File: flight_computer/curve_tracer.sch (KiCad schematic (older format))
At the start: 31 parts

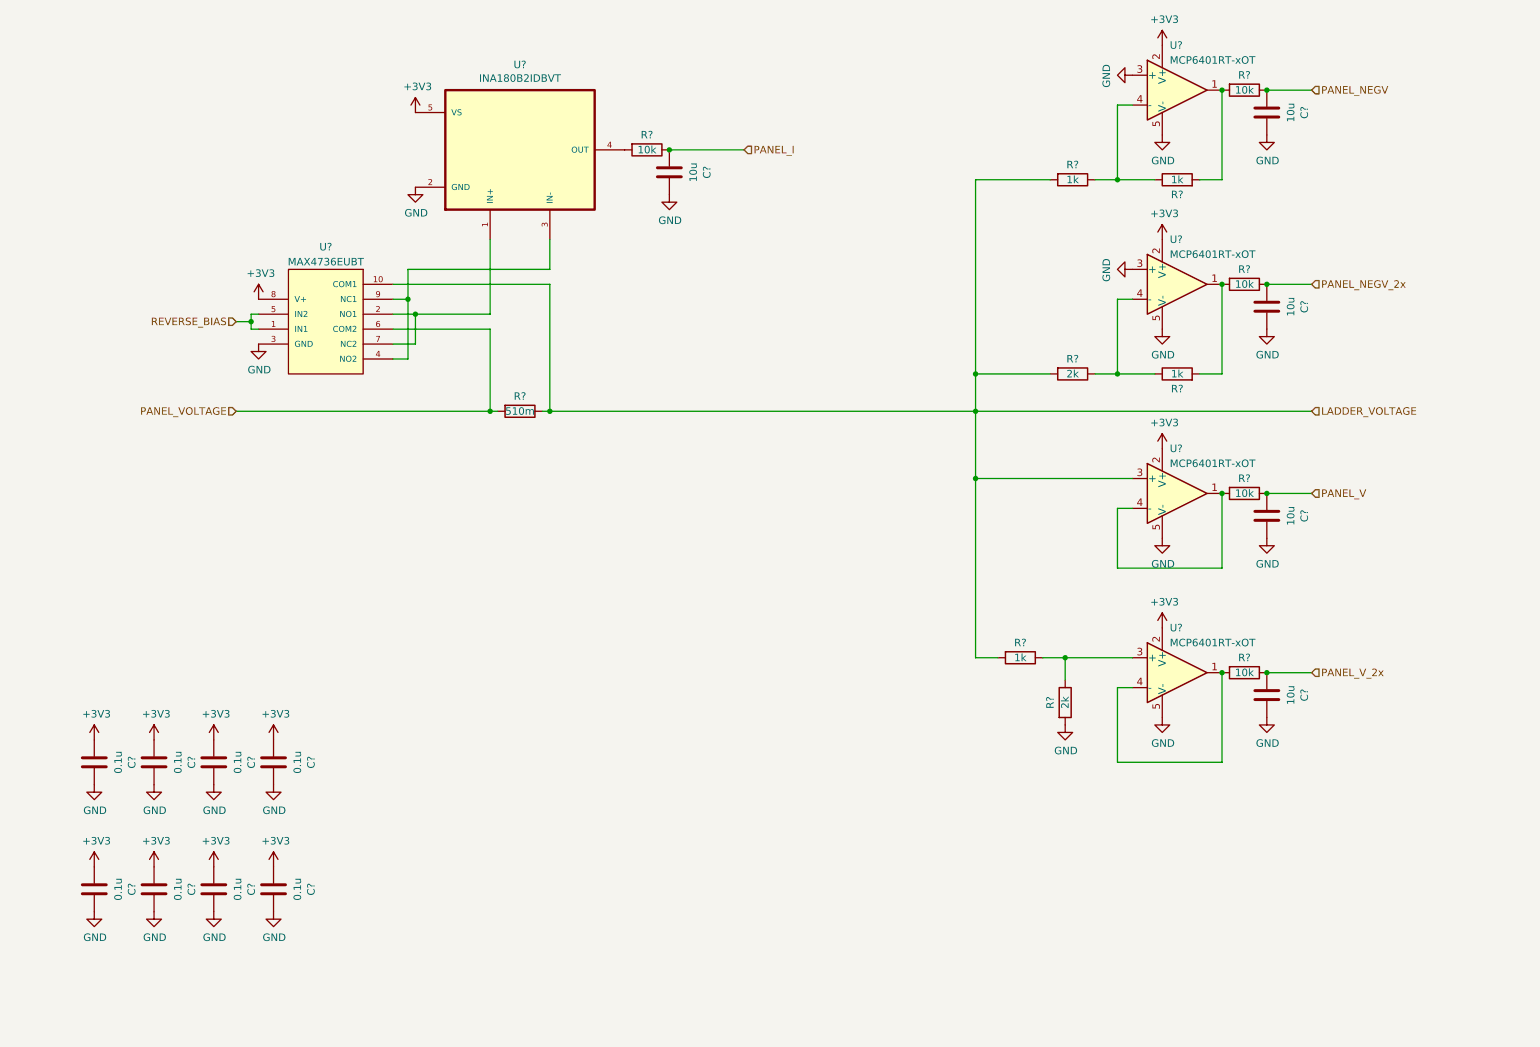
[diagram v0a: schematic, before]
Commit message: Updating flight computer
- Added datasheets for peripherals
- Added resistor ladder firmware
- Added perovskite switcher firmware
- Started flight computer firmware
- Added curve comparisons
- Updating flight computer schematic
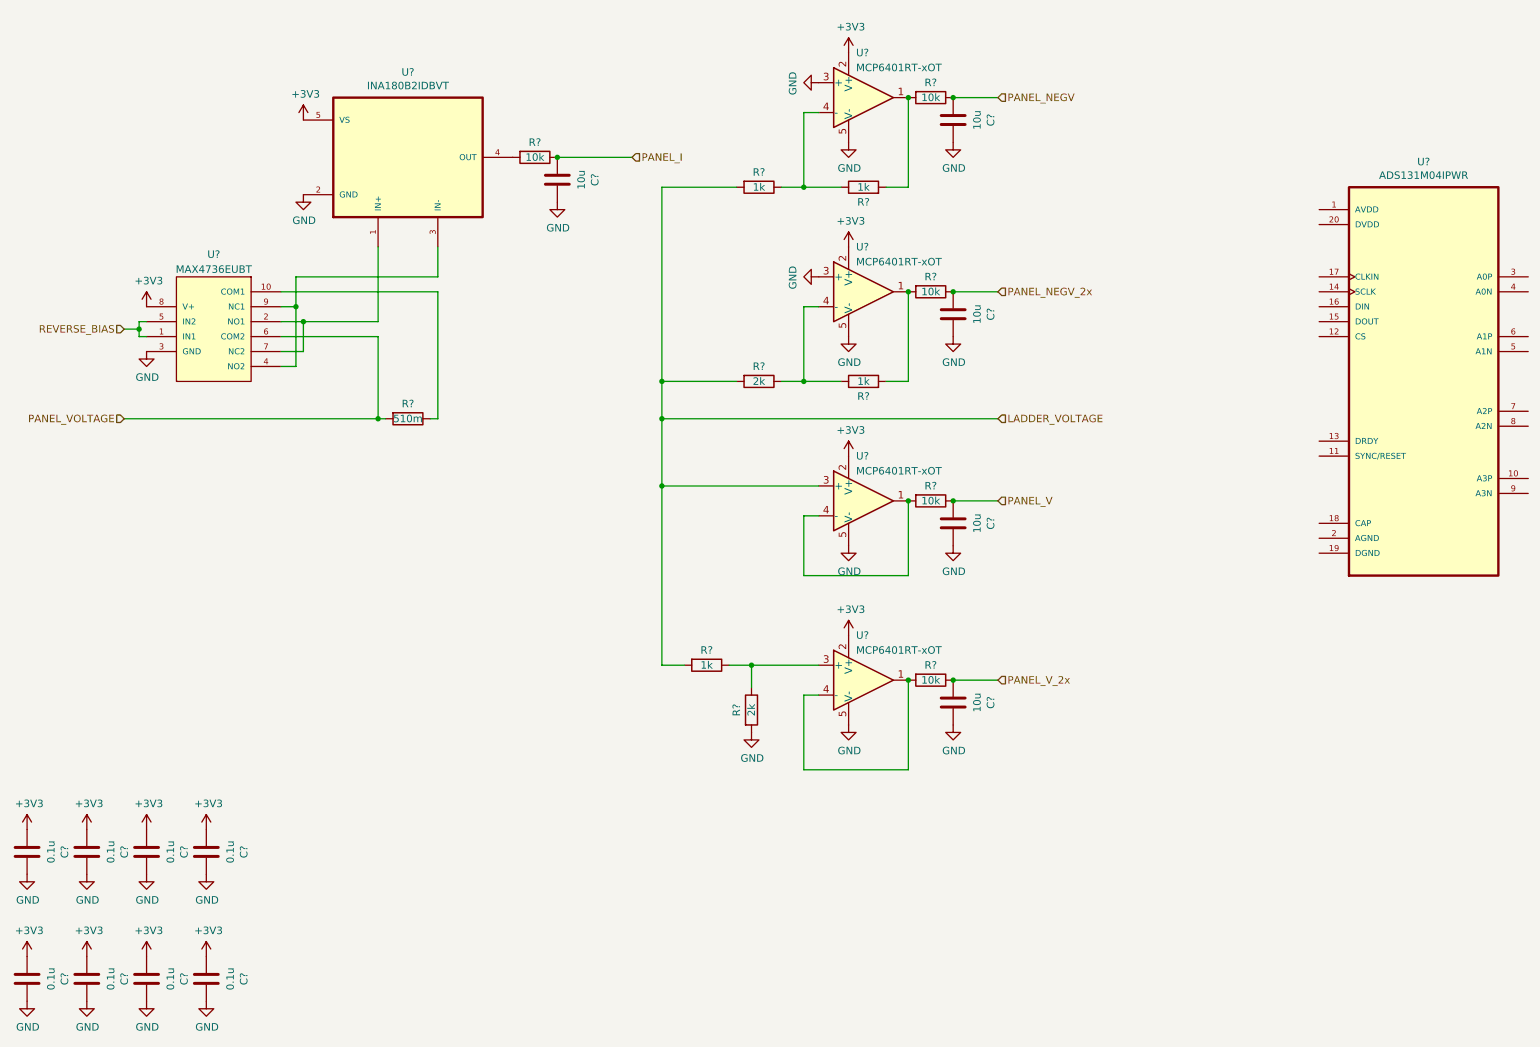
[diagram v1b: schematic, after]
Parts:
- added U?: ADS131M04IPWR, SOP65P640X120-20N, symbol ADS131M04IPWR:ADS131M04IPWR
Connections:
- net LADDER_VOLTAGE: no longer R?.1, U?.10 (COM1)
- new net: R?.1, U?.10 (COM1)
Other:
- moved on the sheet: C?, R?, U?

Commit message: Update flight computer schematic
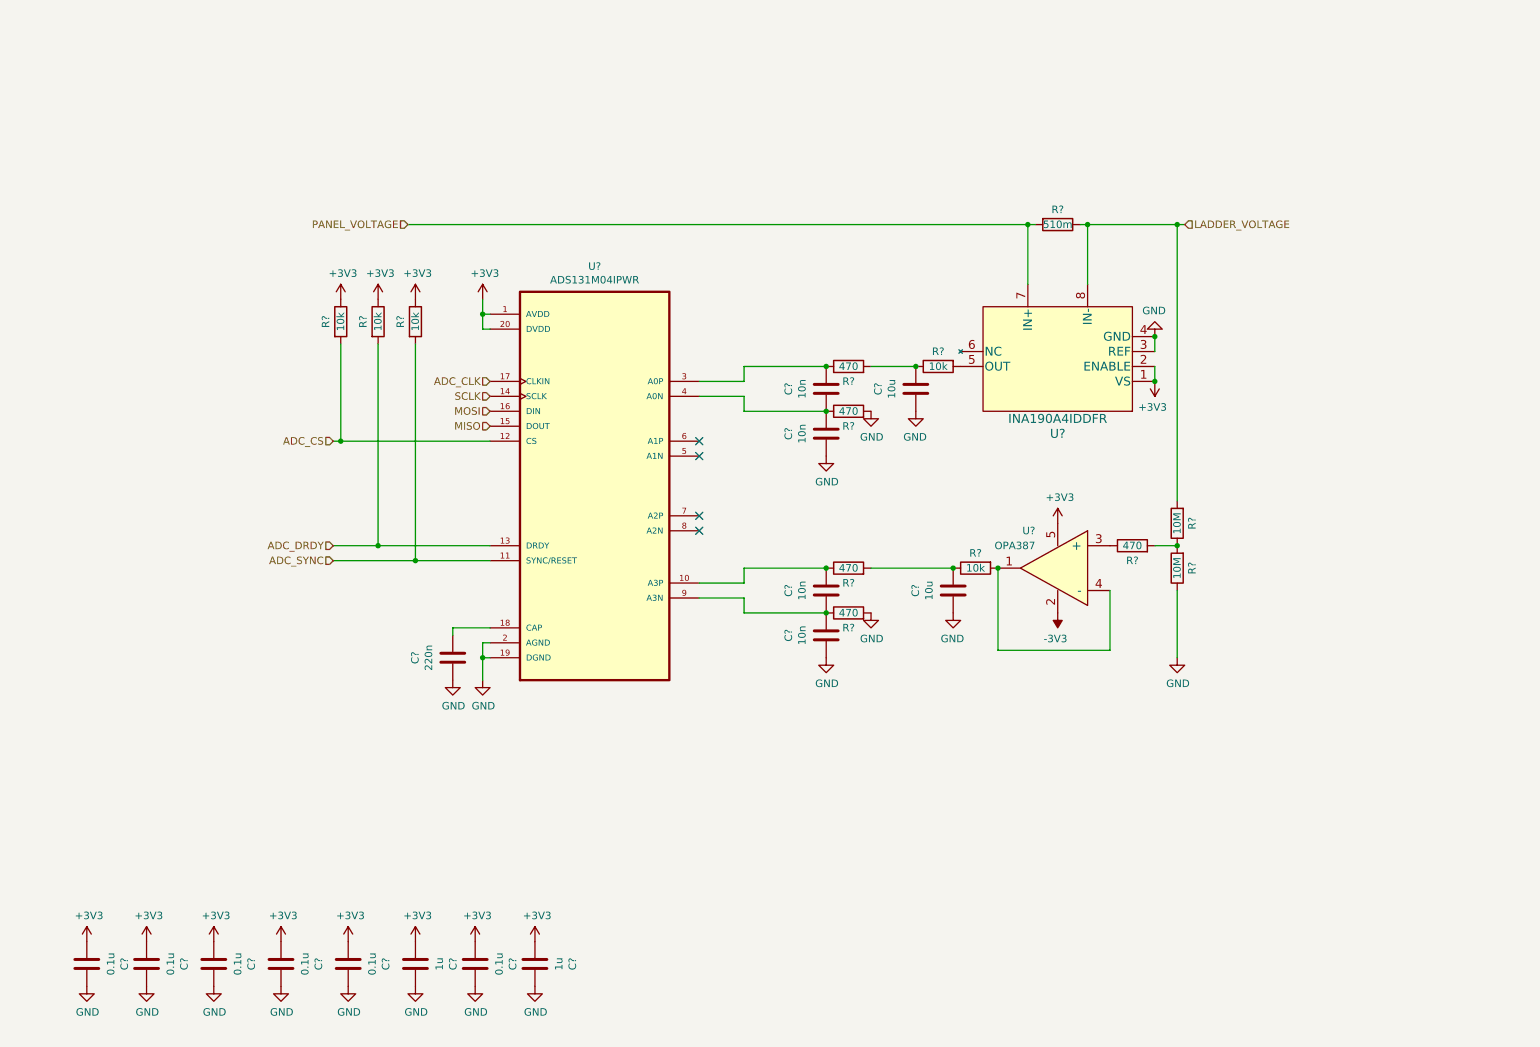
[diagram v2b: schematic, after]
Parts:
- removed C? (x5): 10u, Capacitor_SMD:C_0603_1608Metric, symbol Device:C
- removed R? (x4): 1k, Resistor_SMD:R_0603_1608Metric, symbol Device:R
- removed R? (x5): 10k, Resistor_SMD:R_0603_1608Metric, symbol Device:R
- removed R? (x2): 2k, Resistor_SMD:R_0603_1608Metric, symbol Device:R
- removed U?: INA180B2IDBVT, SOT95P280X145-5N, symbol INA180B2IDBVT:INA180B2IDBVT
- removed U? (x4): MCP6401RT-xOT, Package_TO_SOT_SMD:SOT-23-5, symbol Amplifier_Operational:MCP6401RT-xOT
- removed U?: MAX4736EUBT, MAX4736EUBT:SOP50P490X110-10N, symbol MAX4736EUBT:MAX4736EUBT
- added C? (x2): 10u, Capacitor_SMD:C_0603_1608Metric, symbol Device:C
- added C? (x4): 10n, Capacitor_SMD:C_0603_1608Metric, symbol Device:C
- added C?: 220n, Capacitor_SMD:C_0603_1608Metric, symbol Device:C
- added R? (x5): 10k, Resistor_SMD:R_0603_1608Metric, symbol Device:R
- added R? (x2): 10M, Resistor_SMD:R_0603_1608Metric, symbol Device:R
- added R? (x5): 470, Resistor_SMD:R_0603_1608Metric, symbol Device:R
- added U?: INA190A4IDDFR, GW8-SOT23THIN-DDF-INA190A_TEX, symbol INA190A4IDDFR:INA190A4IDDFR
- added U?: OPA387, symbol OPA387:OPA387
- C? (x2): value 0.1u -> 1u
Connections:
- net +3V3: now also U?.1 (AVDD), U?.20 (DVDD), R?.1, R?.1, R?.1, U?.1 (VS), U?.2 (ENABLE), U?.5
- net GND: now also U?.19 (DGND), U?.2 (AGND), C?.2, C?.2, C?.2, C?.2, C?.2, R?.1, R?.2, R?.2, U?.3 (REF), U?.4 (GND)
- net LADDER_VOLTAGE: now also R?.1, R?.2, U?.8 (IN-)
- net PANEL_VOLTAGE: now also U?.7 (IN+)
- net at U?.10 (A3P): now also C?.1, R?.1
- net ADC_SYNC: now reaches U?.11 (SYNC/RESET)
- net ADC_SYNC: now also R?.2
- net ADC_CS: now reaches U?.12 (CS)
- net ADC_CS: now also R?.2
- net ADC_DRDY: now reaches U?.13 (DRDY)
- net ADC_DRDY: now also R?.2
- net SCLK: now reaches U?.14 (SCLK)
- net MISO: now reaches U?.15 (DOUT)
- net MOSI: now reaches U?.16 (DIN)
- net ADC_CLK: now reaches U?.17 (CLKIN)
- net at U?.18 (CAP): now also C?.1
- net at U?.3 (A0P): now also C?.1, R?.1
- net at U?.4 (A0N): now also C?.1, C?.2, R?.1
- net at U?.9 (A3N): now also C?.1, C?.2, R?.1
- new net: R?.2, U?.5 (OUT)
- new net: R?.2, U?.1, U?.4 (-)
- new net: R?.1, U?.3 (+)
- new net: C?.1, R?.1, R?.2 (x2)
- new net: R?.1, R?.2, R?.2
- new net -3V3: U?.2
- no-connect marks 0 -> 4
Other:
- moved on the sheet: C?, R?, U?

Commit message: Annotating schematic with references and footprints
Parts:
- U12: renamed from U?; footprint SOP65P640X120-20N -> ADS131M04IPWR:SOP65P640X120-20N
- gave numbers to parts that had none: 30

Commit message: Continuing layout
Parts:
- removed C12, C13, C14, C15, C19: 0.1u, Capacitor_SMD:C_0603_1608Metric, symbol Device:C
- removed C17: 1u, Capacitor_SMD:C_0603_1608Metric, symbol Device:C
- removed U14: OPA387, symbol OPA387:OPA387
- added C42: 0.1u, Capacitor_SMD:C_0603_1608Metric, symbol Device:C
- added C43: 1u, Capacitor_SMD:C_0603_1608Metric, symbol Device:C
- added U10: OPA2387, Package_SON:WSON-8-1EP_2x2mm_P0.5mm_EP0.9x1.6mm, symbol OPA2387:OPA2387
- added U31: LT6654AMPS6-1.25, ul_LT6654AMPS6-1-25-TRMPBF:LT6654AMPS6-1.25-TRMPBF, symbol LT6654AMPS6-1.25-TRMPBF:LT6654AMPS6-1.25-TRMPBF
- R24: footprint Resistor_SMD:R_0603_1608Metric -> Resistor_SMD:R_1206_3216Metric
- U13: footprint GW8-SOT23THIN-DDF-INA190A_TEX -> ul_INA190A4IDDFR:INA190A4IDDFR
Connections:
- net +3V3: now also C42.1, U31.4 (VIN)
- net -3V3: now also U10.9 (TP)
- net GND: now also C42.2, C43.2, U31.1 (GND), U31.2 (GND); no longer U13.3 (REF)
- net at R23.2: now also U10.6 (-), U10.7
- net at R25.1: now also U10.5 (+)
- new net: C43.1, U13.3 (REF), U31.6 (VOUT)
